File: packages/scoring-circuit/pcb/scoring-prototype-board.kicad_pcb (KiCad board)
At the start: 2 copper layers, 160 x 100 mm, 36 parts

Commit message: refactor(scoring-circuit): remove retired prototype architecture
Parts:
- added U_CONTROLLER_MODULE: ESP32-S3-DevKitC-1-N8R8, tscircuit:ESP32-S3-DevKitC-1-N8R8, F.Cu at (129.4, 100.0)
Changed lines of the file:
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@@
+  )
+  (footprint
+    "tscircuit:ESP32-S3-DevKitC-1-N8R8"
+    (layer F.Cu)
+    (at 129.43 100 0)
+    (property "Reference" "U_CONTROLLER_MODULE"
+      (at 0 -3 0)
+      (layer F.SilkS)
+      (hide yes)
+      (effects
+        (font
+          (size 1.27 1.27)
+          (thickness 0.15)
+        )
+      )
+    )
+    (property "Value" "ESP32-S3-DevKitC-1-N8R8"
+      (at 0 3 0)
+      (layer F.Fab)
+      (hide yes)
+      (effects
+        (font
+          (size 1.27 1.27)
+          (thickness 0.15)
+        )
+      )
+    )
+    (property "Datasheet" ""
+      (at 0 0 0)
+      (layer F.Fab)
+      (hide yes)
+      (effects
+        (font
+          (size 1.27 1.27)
+          (thickness 0.15)
+        )
+      )
+    )
+    (property "Description" ""
+      (at 0 0 0)
+      (layer F.Fab)
+      (hide yes)
+      (effects
+        (font
+          (size 1.27 1.27)
+          (thickness 0.15)
+        )
+      )
+    )
+    (property "Supplier Part Number" ""
+      (at 0 0 0)
+      (layer F.Fab)
+      (hide yes)
+      (effects
+        (font
+          (size 1.27 1.27)
+          (thickness 0.15)
+        )
+      )
+    )
   )
   (footprint

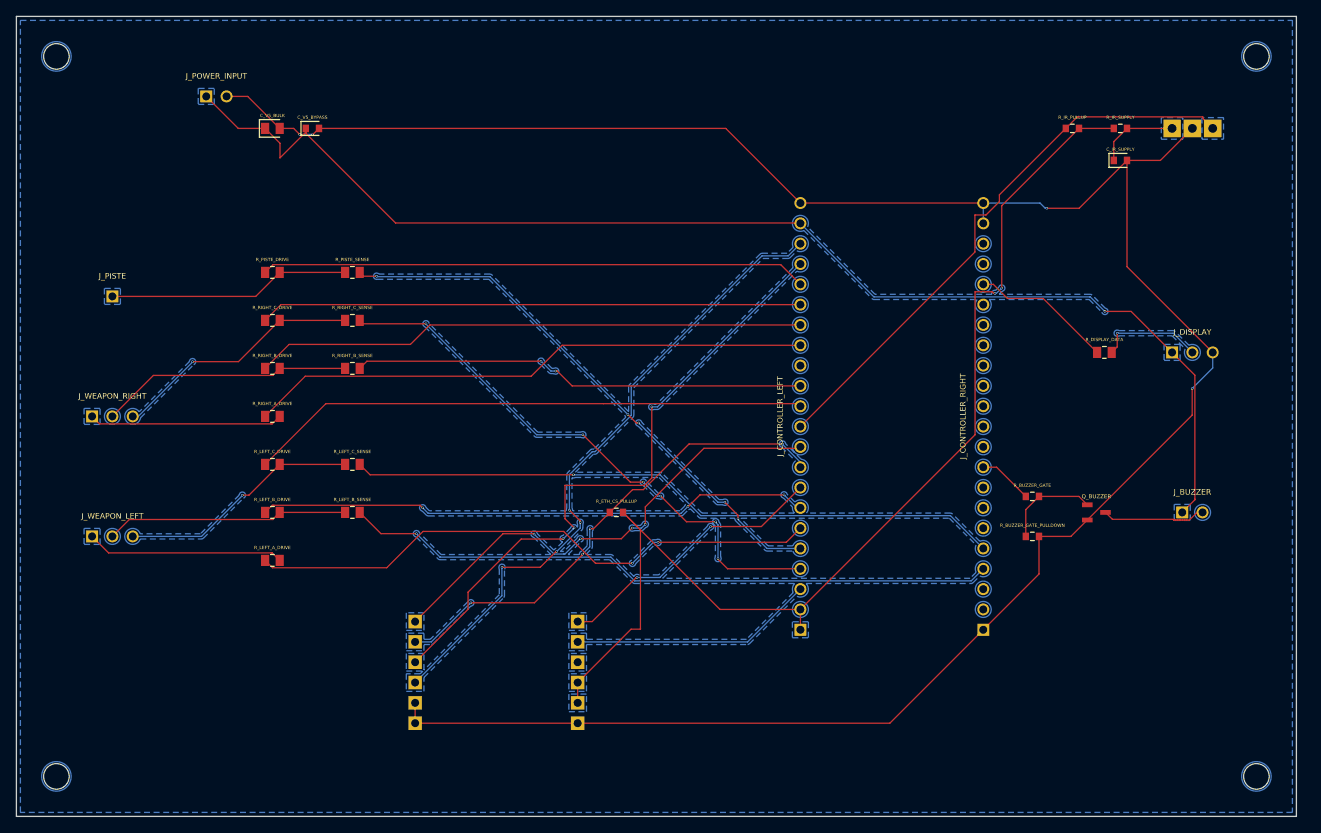
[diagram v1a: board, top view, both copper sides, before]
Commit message: feat(scoring-circuit): add usb-c prototype power
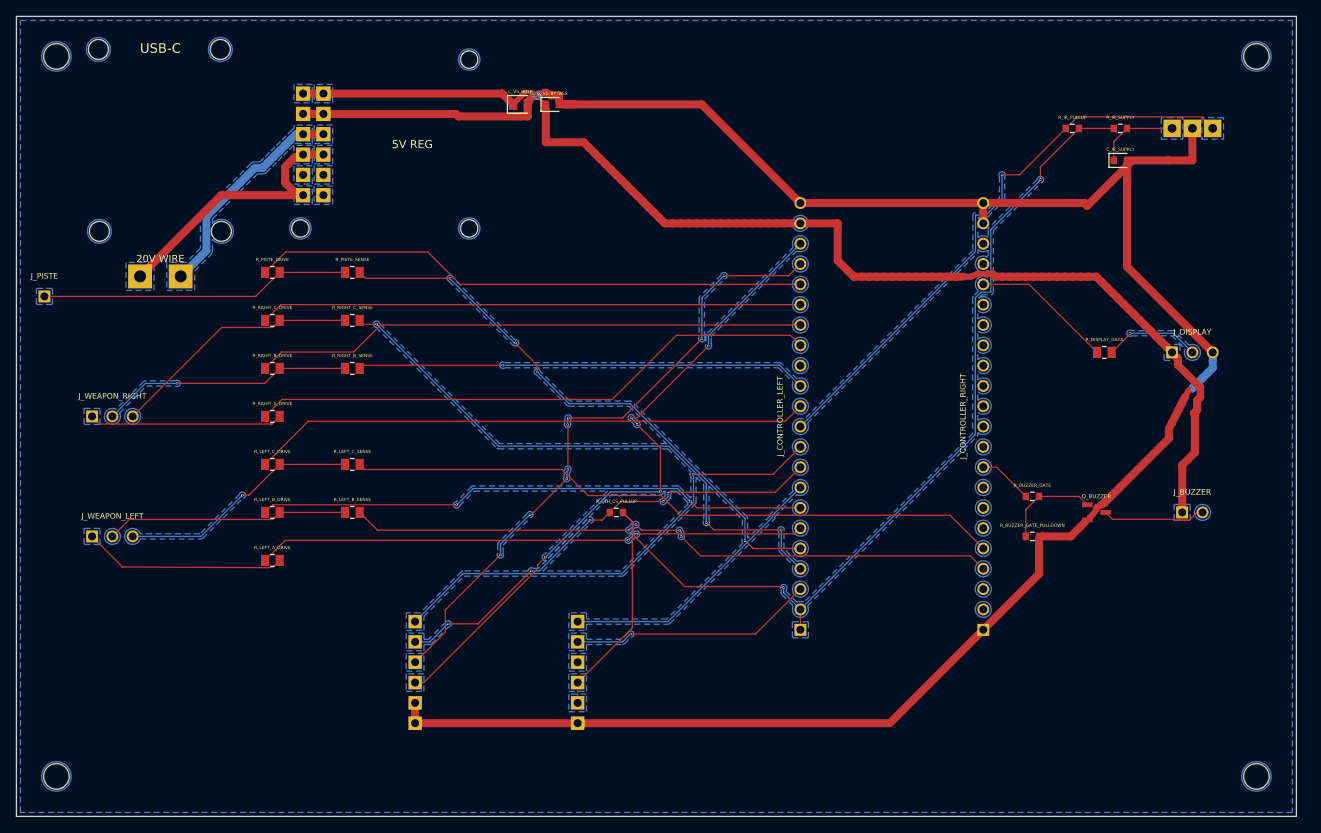
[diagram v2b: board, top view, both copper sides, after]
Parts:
- removed the J_BUZZER at (167.0, 112.0)
- removed the J_DISPLAY at (167.0, 92.0)
- removed the J_PISTE at (32.0, 85.0)
- removed J_POWER_INPUT: J_POWER_INPUT, tscircuit:pin_header_pinrow2_nopinlabels
- added J_BUZZER: J_BUZZER, tscircuit:pin_header, F.Cu at (167.0, 112.0)
- added J_DISPLAY: J_DISPLAY, tscircuit:pin_header, F.Cu at (167.0, 92.0)
- added J_PISTE: J_PISTE, tscircuit:pin_header, F.Cu at (23.5, 85.0)
- added U_USB_C_PD: 5991, tscircuit:5991, F.Cu at (37.9, 68.4)
- added U_V5_REGULATOR: D36V50F5, tscircuit:D36V50F5, F.Cu at (66.0, 65.9)
- J_CONTROLLER_LEFT, J_CONTROLLER_RIGHT: footprint tscircuit:pin_header_pinrow22_nopinlabels -> tscircuit:pin_header
- J_WEAPON_LEFT, J_WEAPON_RIGHT: footprint tscircuit:pin_header_pinrow3_nopinlabels -> tscircuit:pin_header
- moved C_V5_BULK 31.1 mm to (83.0, 61.0)
- moved C_V5_BYPASS 30.1 mm to (87.0, 61.0)
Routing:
- net U_USB_C_PD.PD_20V to U_V5_REGULATOR.VIN_1: track 0.00 -> 35.3 mm
- net U_USB_C_PD.APP_GND to U_V5_REGULATOR.GND_IN_1: track 0.00 -> 27.7 mm
- net V5: track 160.6 -> 151.6 mm, vias 1 -> 0
- net PISTE: track 30.3 -> 38.8 mm
- net APP_GND: track 289.6 -> 285.4 mm, vias 4 -> 3
- net DRIVE_LEFT_A: track 72.6 -> 68.6 mm
- net ETH_CS_N: track 61.3 -> 57.5 mm, vias 4 -> 5
- net SENSE_PISTE: track 69.7 -> 71.6 mm, vias 5 -> 4
- net SENSE_RIGHT_C: track 70.5 -> 72.2 mm, vias 6 -> 3
- net APP_SPI_MOSI: track 80.9 -> 82.5 mm, vias 4 -> 5
- net APP_SPI_SCK: track 80.0 -> 78.6 mm, vias 3 -> 8
- net APP_3V3: track 139.2 -> 137.8 mm
- net DRIVE_PISTE: track 68.3 -> 69.6 mm
- net ETH_INT_N: track 60.6 -> 59.3 mm, vias 4 -> 1
- net IR_RX: track 71.5 -> 72.7 mm, vias 0 -> 1
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
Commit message: feat(scoring-circuit): add scoring indicators
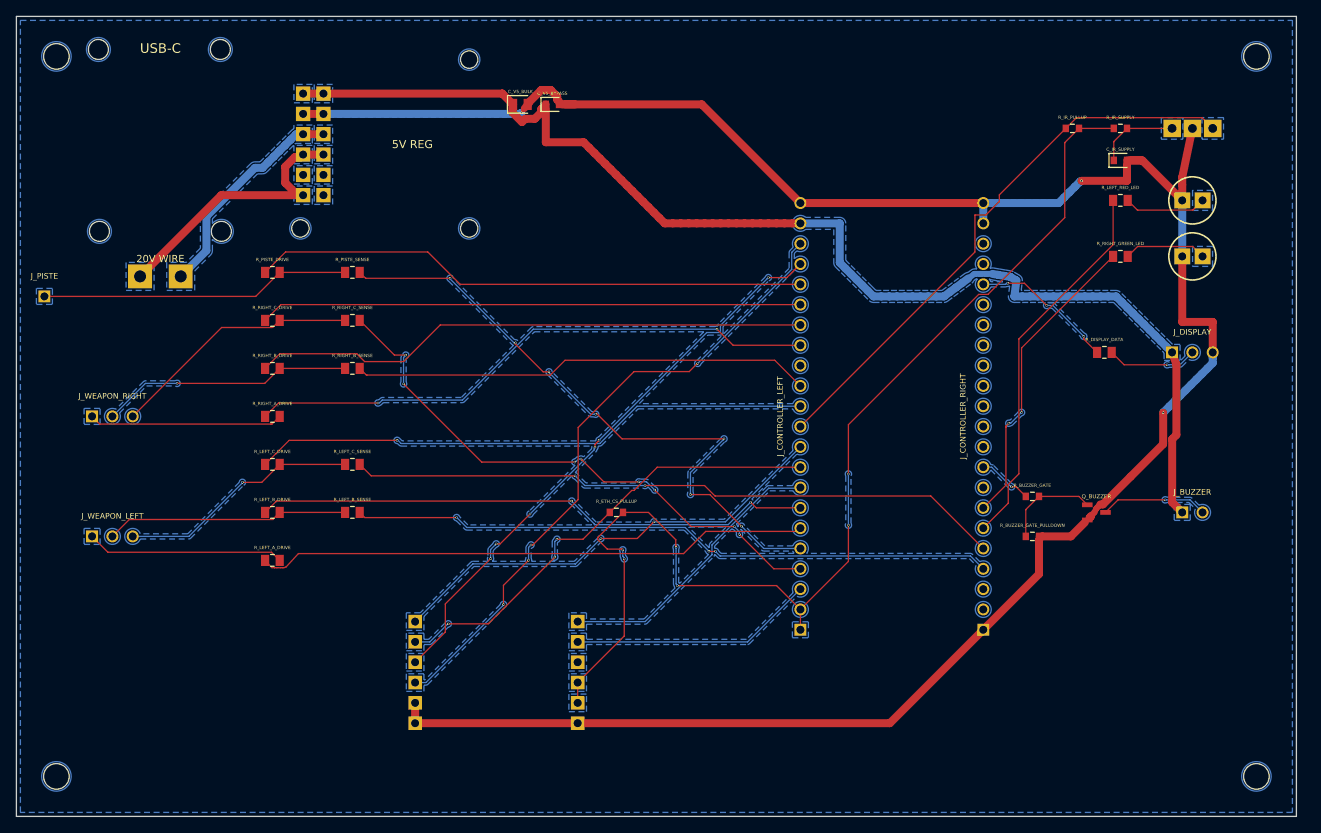
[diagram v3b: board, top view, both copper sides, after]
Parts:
- added LED_LEFT_RED: WP7113ID, tscircuit:WP7113ID, F.Cu at (167.0, 73.0)
- added LED_RIGHT_GREEN: WP7113GD, tscircuit:WP7113GD, F.Cu at (167.0, 80.0)
- added R_LEFT_RED_LED: 330Ω, tscircuit:RC0805FR-07330RL, F.Cu at (158.0, 73.0)
- added R_RIGHT_GREEN_LED: 330Ω, tscircuit:RC0805FR-07330RL, F.Cu at (158.0, 80.0)
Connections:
- J_CONTROLLER_RIGHT pad 6: (no net) -> J_CONTROLLER_RIGHT.6 to R_LEFT_RED_LED.pin1
- J_CONTROLLER_RIGHT pad 7: (no net) -> J_CONTROLLER_RIGHT.7 to R_RIGHT_GREEN_LED.pin1
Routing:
- net J_CONTROLLER_RIGHT.6 to R_LEFT_RED_LED.pin1: track 0.00 -> 47.7 mm
- net J_CONTROLLER_RIGHT.7 to R_RIGHT_GREEN_LED.pin1: track 0.00 -> 38.3 mm, vias 0 -> 2
- net R_RIGHT_GREEN_LED.pin2 to LED_RIGHT_GREEN.anode: track 0.00 -> 10.4 mm
- net R_LEFT_RED_LED.pin2 to LED_LEFT_RED.anode: track 0.00 -> 10.4 mm
- net SENSE_PISTE: track 71.6 -> 79.7 mm, vias 4 -> 7
- net APP_SPI_SCK: track 78.6 -> 72.4 mm, vias 8 -> 6
- net APP_3V3: track 137.8 -> 142.6 mm, vias 2 -> 6
- net V5: track 151.6 -> 154.8 mm
- net APP_SPI_MOSI: track 82.5 -> 79.8 mm, vias 5 -> 4
- net ETH_INT_N: track 59.3 -> 57.2 mm, vias 1 -> 2
- net IR_RX: track 72.7 -> 71.3 mm, vias 1 -> 0
- net SENSE_RIGHT_C: track 72.2 -> 71.0 mm, vias 3 -> 8
- net SENSE_RIGHT_B: track 56.3 -> 57.5 mm, vias 1 -> 0
- net DRIVE_LEFT_B: track 69.1 -> 70.2 mm
- net SENSE_LEFT_B: track 81.8 -> 80.9 mm, vias 4 -> 3
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
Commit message: feat(scoring-circuit): add prototype sounder
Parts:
- BZ_SCORING: renamed from J_BUZZER; value J_BUZZER -> PS1240P02BT; footprint tscircuit:pin_header -> tscircuit:PS1240P02BT
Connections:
- net J_BUZZER.BUZZER_SWITCHED_GND to Q_BUZZER.DRAIN renamed BZ_SCORING.SWITCHED_GROUND to Q_BUZZER.DRAIN
- BZ_SCORING pad 1: V5 -> APP_3V3
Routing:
- net APP_3V3: track 142.6 -> 170.6 mm, vias 6 -> 5
- net V5: track 154.8 -> 128.5 mm, vias 0 -> 1
- net APP_GND: track 285.3 -> 288.2 mm
- net DISPLAY_DATA: track 18.1 -> 20.7 mm, vias 3 -> 2
- net BZ_SCORING.SWITCHED_GROUND to Q_BUZZER.DRAIN: track 13.4 -> 14.4 mm, vias 1 -> 0
- net J_CONTROLLER_RIGHT.6 to R_LEFT_RED_LED.pin1: vias 0 -> 2

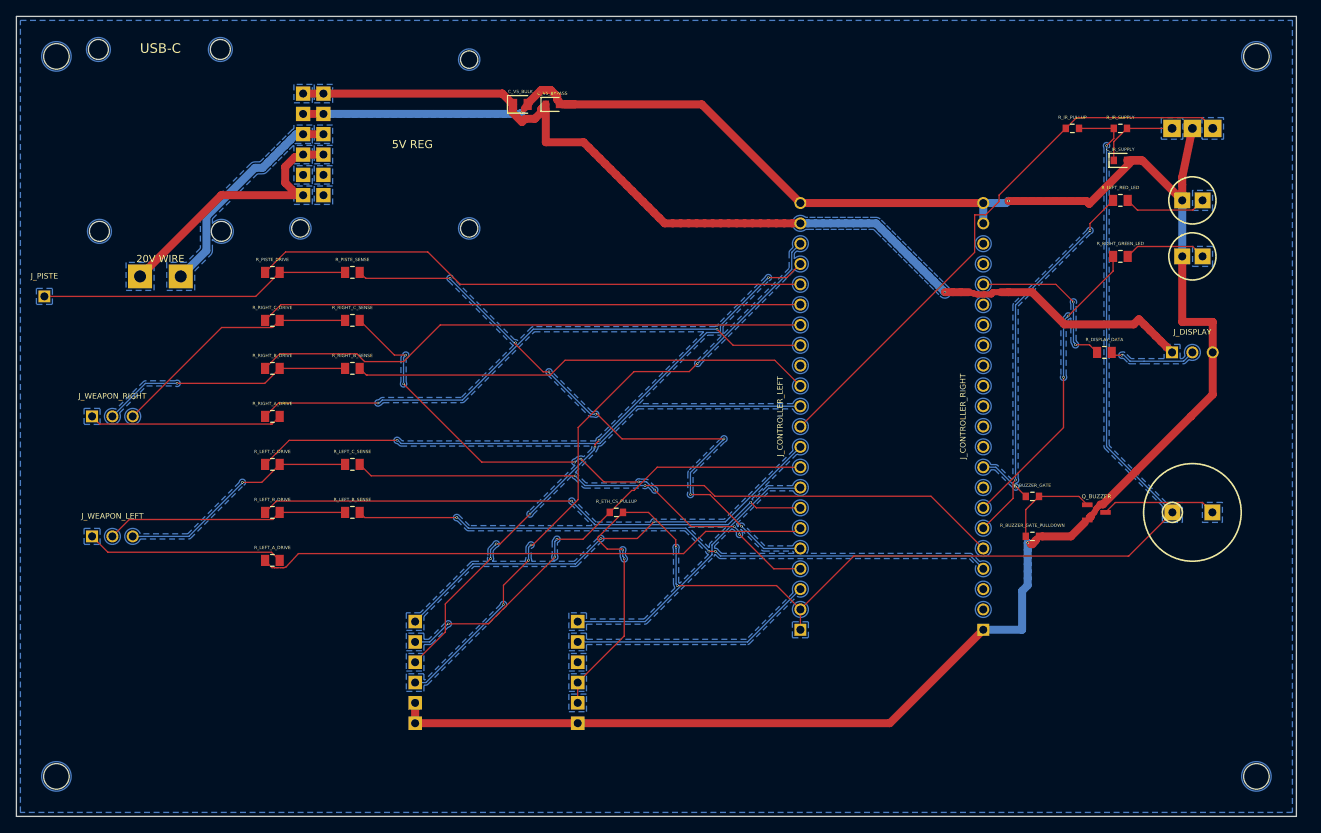
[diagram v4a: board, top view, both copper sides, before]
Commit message: feat(scoring-circuit): add repeater outputs
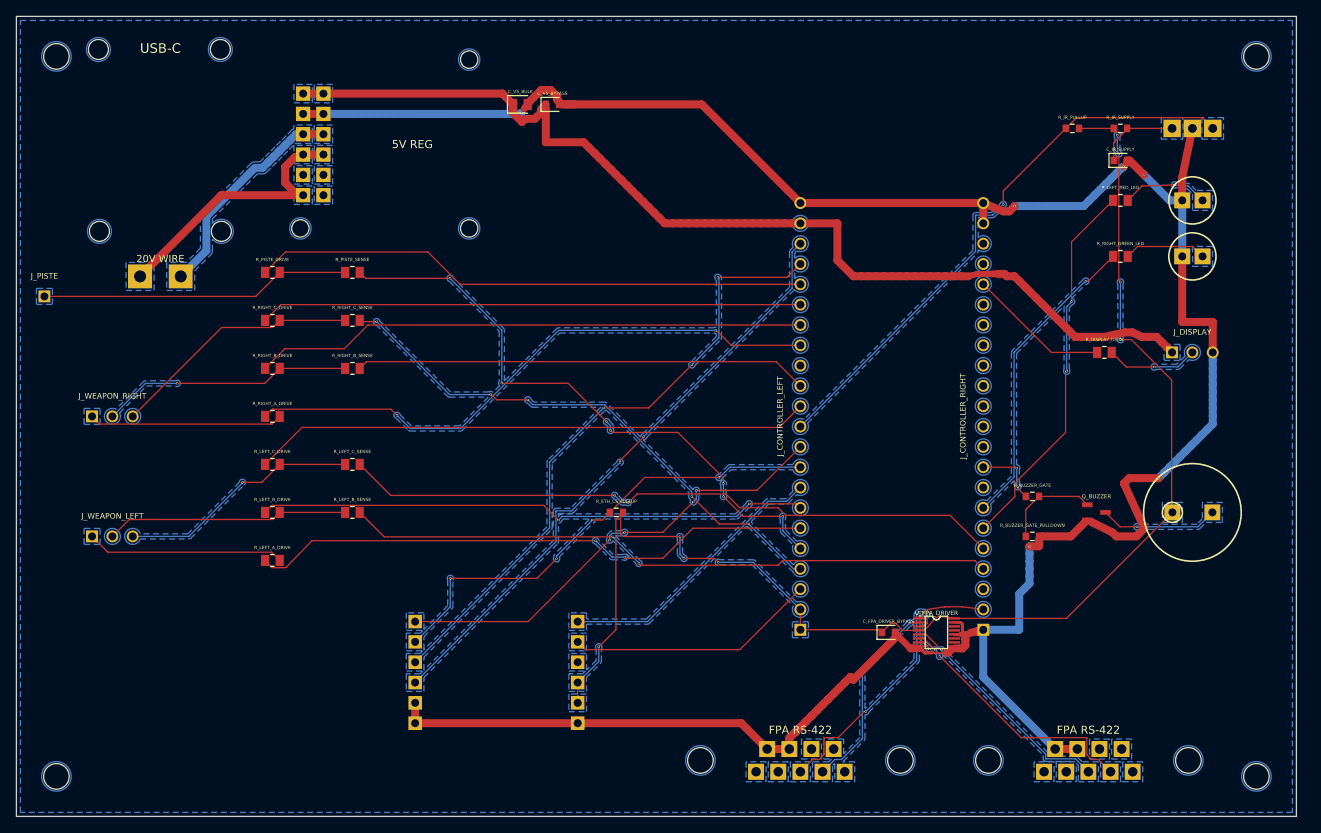
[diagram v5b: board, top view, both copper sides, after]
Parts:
- added C_FPA_DRIVER_BYPASS: 100nF, tscircuit:C0603C104K3RACTU, F.Cu at (129.0, 127.0)
- added J_FPA_REPEATER_1: 182-009-113R161, tscircuit:182-009-113R161, F.Cu at (118.0, 143.0)
- added J_FPA_REPEATER_2: 182-009-113R161, tscircuit:182-009-113R161, F.Cu at (154.0, 143.0)
- added U_FPA_DRIVER: AM26LV31EIPWR, tscircuit:AM26LV31EIPWR, F.Cu at (135.0, 127.0)
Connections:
- J_CONTROLLER_RIGHT pad 2: (no net) -> FPA_TX
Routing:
- net APP_GND: track 288.2 -> 333.2 mm, vias 3 -> 6
- net U_FPA_DRIVER.DRIVER_2_POSITIVE to J_FPA_REPEATER_2.TX_POS: track 0.00 -> 32.3 mm, vias 0 -> 2
- net U_FPA_DRIVER.DRIVER_1_NEGATIVE to J_FPA_REPEATER_1.TX_NEG: track 0.00 -> 31.3 mm, vias 0 -> 2
- net U_FPA_DRIVER.DRIVER_2_NEGATIVE to J_FPA_REPEATER_2.TX_NEG: track 0.00 -> 28.7 mm, vias 0 -> 1
- net U_FPA_DRIVER.DRIVER_1_POSITIVE to J_FPA_REPEATER_1.TX_POS: track 0.00 -> 24.7 mm, vias 0 -> 1
- net FPA_TX: track 0.00 -> 15.6 mm, vias 0 -> 2
- net APP_SPI_SCK: track 72.4 -> 78.2 mm, vias 6 -> 3
- net APP_SPI_MOSI: track 79.8 -> 75.9 mm, vias 4 -> 2
- net SENSE_PISTE: track 79.7 -> 76.1 mm
- net DISPLAY_DATA: track 20.7 -> 17.8 mm, vias 2 -> 0
- net SENSE_RIGHT_C: track 71.0 -> 68.3 mm, vias 8 -> 5
- net V5: track 128.5 -> 130.8 mm, vias 1 -> 0
- net DRIVE_LEFT_A: track 69.4 -> 71.3 mm, vias 0 -> 2
- net DRIVE_RIGHT_A: track 72.3 -> 74.1 mm
- net APP_3V3: track 170.6 -> 169.0 mm, vias 5 -> 8
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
